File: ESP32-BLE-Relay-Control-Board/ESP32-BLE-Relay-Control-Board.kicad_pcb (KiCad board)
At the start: 2 copper layers, 13 parts, among them K1 SANYOU_SRD_Form_C, Q1 BC817, SW1 SW_Push, SW2 SW_Push, U1 ESP32-WROOM-32, U2 EL817

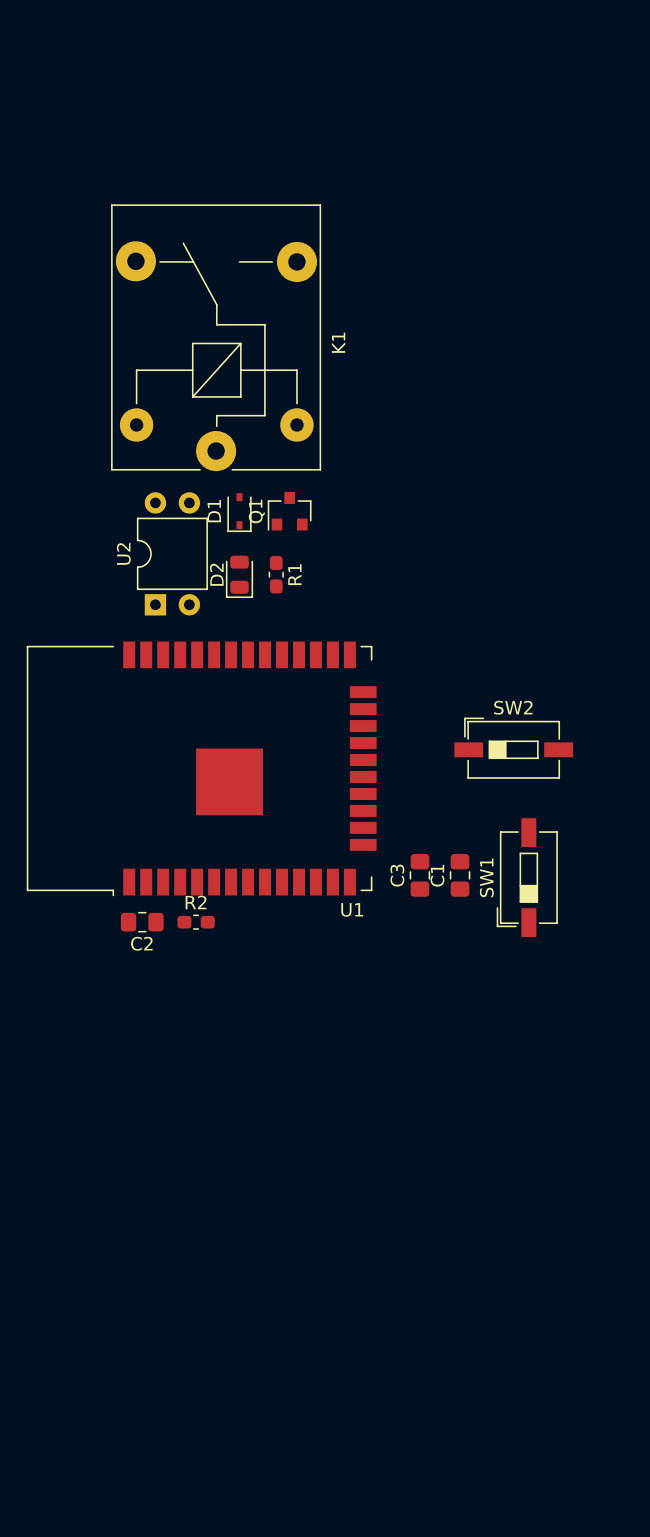
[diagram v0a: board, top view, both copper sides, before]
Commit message: relay added
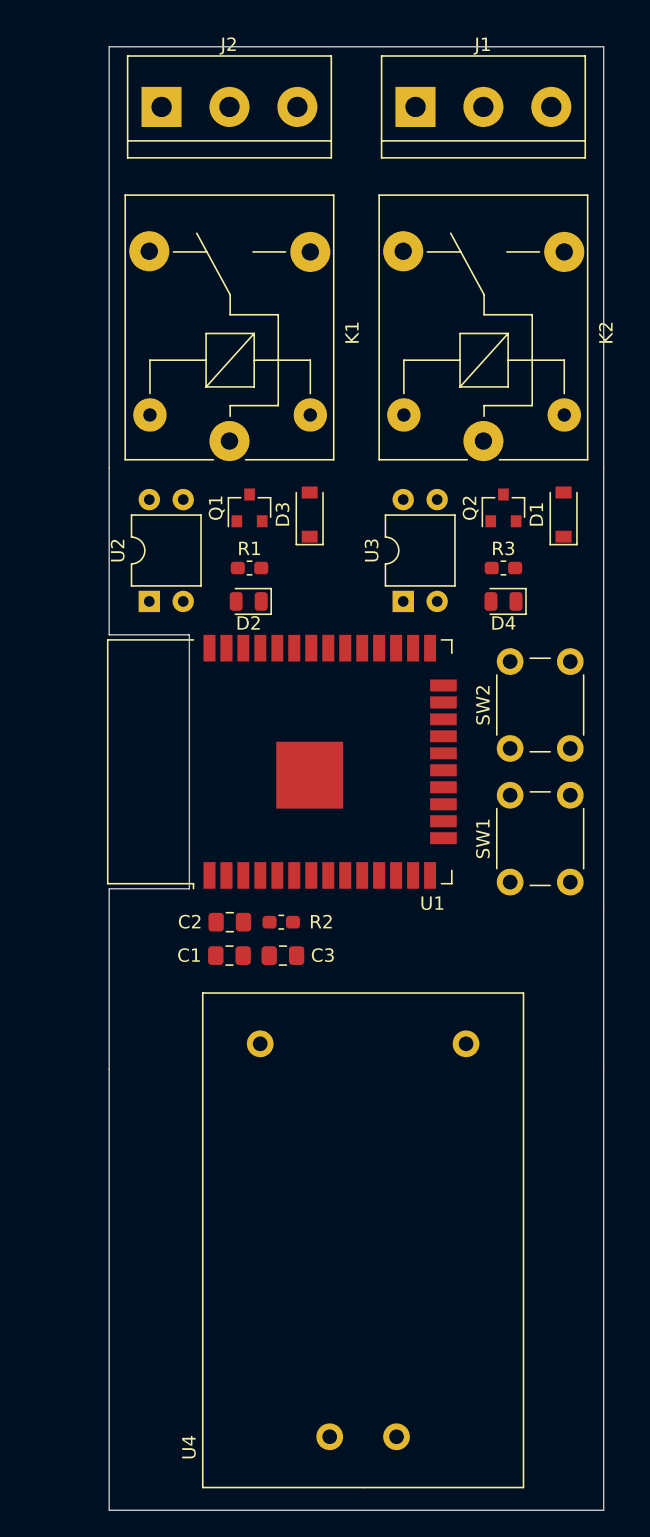
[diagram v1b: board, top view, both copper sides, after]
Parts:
- added D3: 1N4148W, Diode_SMD:D_SOD-123, F.Cu at (115.0, 103.5)
- added D4: LED, LED_SMD:LED_0805_2012Metric, F.Cu at (129.5, 110.0)
- added J1: Conn_01x03, TerminalBlock:TerminalBlock_bornier-3_P5.08mm, F.Cu at (122.9, 73.0)
- added J2: Conn_01x03, TerminalBlock:TerminalBlock_bornier-3_P5.08mm, F.Cu at (103.9, 73.0)
- added K2: SANYOU_SRD_Form_C, Relay_THT:Relay_SPDT_SANYOU_SRD_Series_Form_C, F.Cu at (128.0, 98.0)
- added Q2: BC817, Package_TO_SOT_SMD:SOT-23, F.Cu at (129.5, 103.0)
- added R3: R_Small, Resistor_SMD:R_0603_1608Metric_Pad1.05x0.95mm_HandSolder, F.Cu at (129.5, 107.5)
- added U3: EL817, Package_DIP:DIP-4_W7.62mm, F.Cu at (122.0, 110.0)
- added U4: easyPower-5V, electroShri:easyPower-5V, F.Cu at (119.0, 176.3)
- D1: value 1N4148WS -> 1N4148W; footprint Diode_SMD:D_SOD-323 -> Diode_SMD:D_SOD-123
- SW1, SW2: footprint Button_Switch_SMD:SW_DIP_SPSTx01_Slide_6.7x4.1mm_W6.73mm_P2.54mm_LowProfile_JPin -> Button_Switch_THT:SW_PUSH_6mm
- moved D1 24.3 mm to (134.0, 103.5)
- moved C1 18.3 mm to (109.0, 136.5), turned to 180 degrees
- moved C3 11.9 mm to (113.0, 136.5), turned to 0 degrees
- moved C2 6.55 mm to (109.0, 134.0)
- moved R2 6.38 mm to (112.9, 134.0)
- moved U1 6.02 mm to (115.8, 122.0)
- moved Q1 3.01 mm to (110.5, 103.0)
- moved D2 2.11 mm to (110.4, 110.0), turned to 180 degrees
- moved R1 2.06 mm to (110.5, 107.5), turned to 0 degrees
- moved SW1 1.44 mm to (130.0, 131.0)
- moved K1 1.25 mm to (109.0, 98.0)
- moved U2 0.52 mm to (103.0, 110.0)
- moved SW2 0.28 mm to (130.0, 121.0), turned to 90 degrees
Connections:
- K1 pad 1: Net-(K1-Pad1) -> /COM_2
- K1 pad 2: Net-(D1-Pad2) -> Net-(D3-Pad2)
- Q1 pad 3: Net-(D1-Pad2) -> Net-(D3-Pad2)
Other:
- board outline added: 37 x 109.5 mm

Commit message: Power in connector added
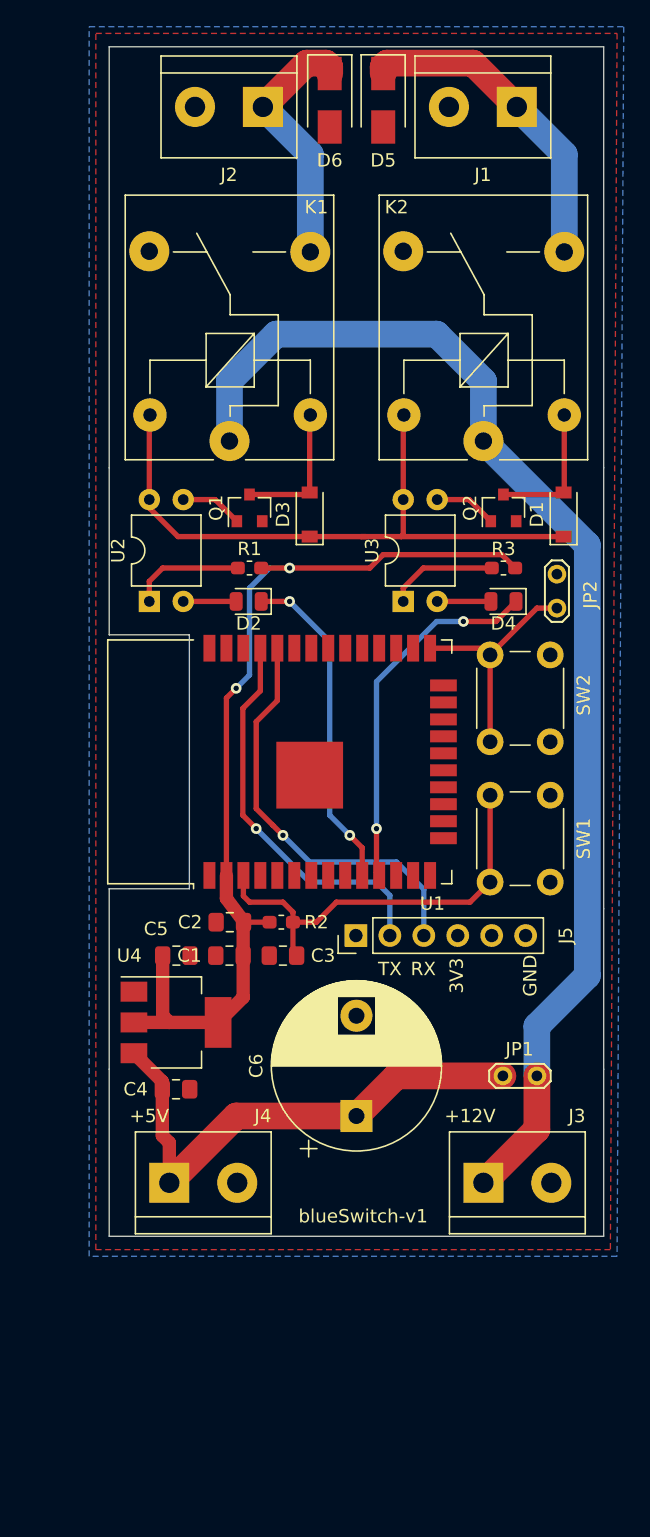
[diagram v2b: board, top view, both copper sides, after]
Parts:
- added C4: C_Small, Capacitor_SMD:C_0805_2012Metric_Pad1.15x1.40mm_HandSolder, F.Cu at (105.0, 146.5)
- added C5: C_Small, Capacitor_SMD:C_0805_2012Metric_Pad1.15x1.40mm_HandSolder, F.Cu at (105.0, 136.5)
- added C6: CP1, Capacitor_THT:CP_Radial_D12.5mm_P7.50mm, F.Cu at (118.5, 148.5)
- added D5: US1M, Diode_SMD:D_SMA, F.Cu at (120.5, 72.5)
- added D6: US1M, Diode_SMD:D_SMA, F.Cu at (116.5, 72.5)
- added J3: Screw_Terminal_01x02, TerminalBlock:TerminalBlock_bornier-2_P5.08mm, F.Cu at (128.0, 153.5)
- added J4: Screw_Terminal_01x02, TerminalBlock:TerminalBlock_bornier-2_P5.08mm, F.Cu at (104.5, 153.5)
- added J5: Conn_01x06_Female, Connector_PinHeader_2.54mm:PinHeader_1x06_P2.54mm_Vertical, F.Cu at (118.5, 135.0)
- added JP1: Jumper, TestPoint:TestPoint_2Pads_Pitch2.54mm_Drill0.8mm, F.Cu at (132.0, 145.5)
- added JP2: Jumper, TestPoint:TestPoint_2Pads_Pitch2.54mm_Drill0.8mm, F.Cu at (133.5, 110.5)
- J1, J2: value Conn_01x03 -> Screw_Terminal_01x02; footprint TerminalBlock:TerminalBlock_bornier-3_P5.08mm -> TerminalBlock:TerminalBlock_bornier-2_P5.08mm
- U4: value easyPower-5V -> LM1117-3.3; footprint electroShri:easyPower-5V -> Package_TO_SOT_SMD:SOT-223-3_TabPin2
- moved U4 37.5 mm to (105.0, 141.5), turned to 0 degrees
- moved J1 7.58 mm to (130.5, 73.0), turned to 180 degrees
- moved J2 7.58 mm to (111.5, 73.0), turned to 180 degrees
- moved SW2 1.58 mm to (128.5, 120.5)
- moved SW1 1.50 mm to (128.5, 131.0)
- turned C3 to 180 degrees
- turned R2 to 180 degrees
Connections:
- D2 pad 1: /IN1 -> IO25
- D4 pad 1: /IN2 -> IO26
- J1 pad 1: Net-(J1-Pad1) -> Net-(D5-Pad1)
- J1 pad 2: /COM_1 -> GND
- J2 pad 1: Net-(J2-Pad1) -> Net-(D6-Pad1)
- J2 pad 2: /COM_2 -> GND
- K1 pad 1: /COM_2 -> +12V
- K1 pad 3: Net-(J2-Pad3) -> Net-(D6-Pad1)
- K1 pad 4: Net-(J2-Pad1) -> Net-(K1-Pad4)
- K2 pad 1: /COM_1 -> +12V
- K2 pad 3: Net-(J1-Pad3) -> Net-(D5-Pad1)
- K2 pad 4: Net-(J1-Pad1) -> Net-(K2-Pad4)
- R1 pad 2: +5V -> +3V3
- R3 pad 2: +5V -> +3V3
- U1 pad 10: Net-(U1-Pad10) -> IO25
- U1 pad 11: Net-(U1-Pad11) -> IO26
- U1 pad 34: /RX0 -> RX0
- U1 pad 35: /TX0 -> TX0
- U4 pad 1: Net-(U4-Pad1) -> GND
- U4 pad 2: Net-(U4-Pad2) -> +3V3
- U4 pad 3: Net-(U4-Pad3) -> +5V
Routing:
- net +12V: track 0.00 -> 92.8 mm
- net +3V3: track 0.00 -> 82.6 mm, vias 0 -> 2
- net VCCQ: track 0.00 -> 48.4 mm
- net +5V: track 0.00 -> 39.1 mm
- net /EN: track 0.00 -> 31.6 mm
- net RX0: track 0.00 -> 31.2 mm, vias 0 -> 1
- net TX0: track 0.00 -> 29.5 mm, vias 0 -> 1
- net IO26: track 0.00 -> 27.5 mm, vias 0 -> 2
- net IO25: track 0.00 -> 24.9 mm, vias 0 -> 2
- net Net-(D5-Pad1): track 0.00 -> 24.3 mm
- net Net-(D6-Pad1): track 0.00 -> 19.3 mm
- net /IO0: track 0.00 -> 17.6 mm
- net Net-(D1-Pad2): track 0.00 -> 10.4 mm
- net Net-(D3-Pad2): track 0.00 -> 10.4 mm
- net Net-(R1-Pad1): track 0.00 -> 8.54 mm
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- added copper zone on B.Cu, net GND
- added copper zone on F.Cu, net GND
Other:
- board size 37 x 109.5 mm -> 37 x 89 mm
- board text added: "+12V"
- board text added: "+5V"
- board text added: "3V3"
- board text added: "GND"
- board text added: "RX"
- board text added: "TX"
- board text added: "blueSwitch-v1"

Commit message: 5V LDO Added
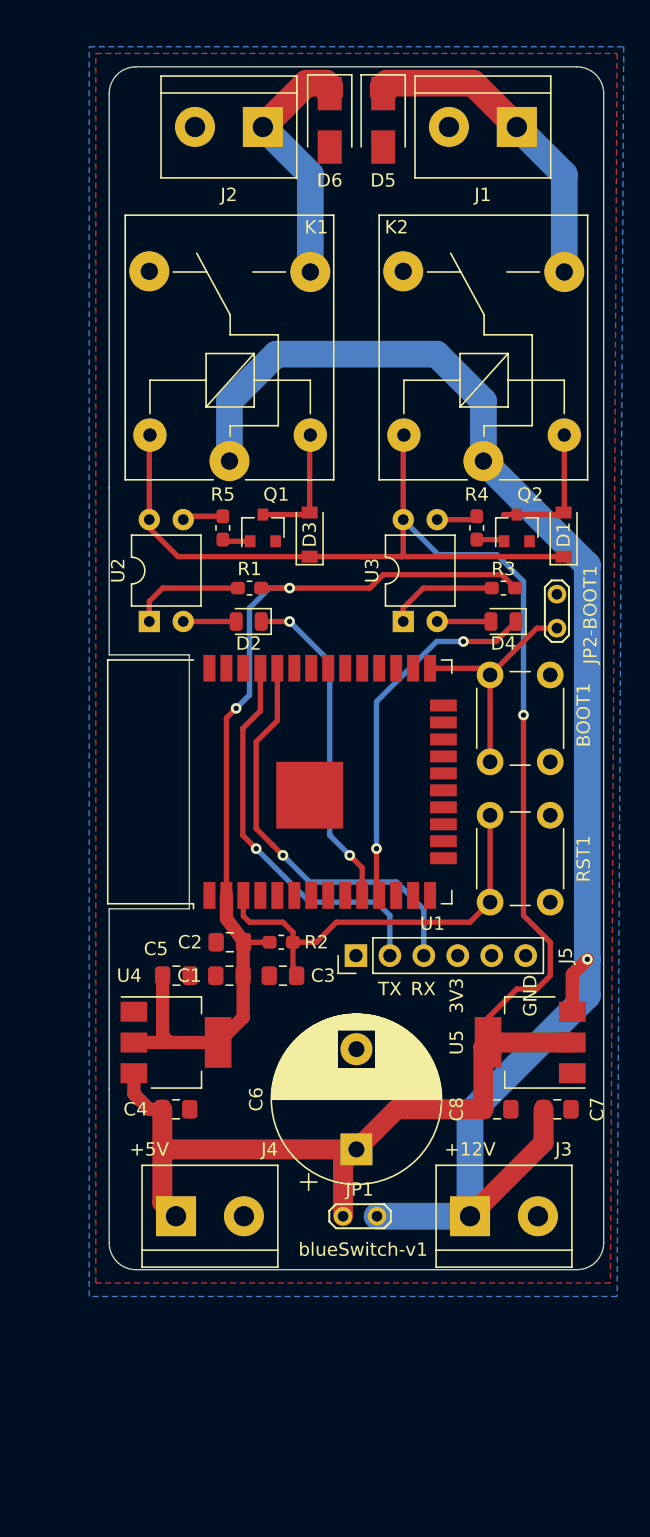
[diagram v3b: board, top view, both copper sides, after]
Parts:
- added C7: 1uF, Capacitor_SMD:C_0805_2012Metric_Pad1.15x1.40mm_HandSolder, F.Cu at (133.5, 148.0)
- added C8: 1uF, Capacitor_SMD:C_0805_2012Metric_Pad1.15x1.40mm_HandSolder, F.Cu at (129.0, 148.0)
- added R4: 500, Resistor_SMD:R_0603_1608Metric_Pad1.05x0.95mm_HandSolder, F.Cu at (127.5, 104.5)
- added R5: 500, Resistor_SMD:R_0603_1608Metric_Pad1.05x0.95mm_HandSolder, F.Cu at (108.5, 104.5)
- added U5: LM1117-5.0, Package_TO_SOT_SMD:SOT-223-3_TabPin2, F.Cu at (131.5, 143.0)
- C1, C2: value C_Small -> 0.1uF
- C4, C5: value C_Small -> 1uF
- moved JP1 15.9 mm to (120.0, 156.0)
- moved J3 2.69 mm to (127.0, 156.0)
- moved J4 2.55 mm to (105.0, 156.0)
- moved C6 2.50 mm to (118.5, 151.0)
- moved Q1 1.80 mm to (111.5, 104.5)
- moved Q2 1.80 mm to (130.5, 104.5)
- moved BOOT1 1.50 mm to (128.5, 122.0)
- moved C1 1.50 mm to (109.0, 138.0)
- moved C2 1.50 mm to (109.0, 135.5)
- moved C3 1.50 mm to (113.0, 138.0)
- moved C4 1.50 mm to (105.0, 148.0)
- moved C5 1.50 mm to (105.0, 138.0)
- moved D1 1.50 mm to (134.0, 105.0)
- moved D2 1.50 mm to (110.4, 111.5)
- moved D3 1.50 mm to (115.0, 105.0)
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- renumbered SW2 to BOOT1, JP2 to JP2-BOOT1, SW1 to RST1
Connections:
- D1 pad 1: VCCQ -> +5V
- D3 pad 1: VCCQ -> +5V
- K1 pad 5: VCCQ -> +5V
- K2 pad 5: VCCQ -> +5V
- U2 pad 3: Net-(Q1-Pad1) -> Net-(R5-Pad2)
- U2 pad 4: VCCQ -> +5V
- U3 pad 3: Net-(Q2-Pad1) -> Net-(R4-Pad2)
- U3 pad 4: VCCQ -> +5V
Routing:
- net +5V: track 39.1 -> 152.2 mm, vias 0 -> 1
- net VCCQ: track 48.4 -> 0.00 mm
- net +12V: track 92.8 -> 115.9 mm, vias 0 -> 1
- net Net-(R5-Pad2): track 0.00 -> 3.07 mm
- net Net-(R4-Pad2): track 0.00 -> 3.07 mm
- net Net-(Q1-Pad1): track 4.68 -> 2.10 mm
- net Net-(Q2-Pad1): track 4.68 -> 2.10 mm
- net Net-(D3-Pad2): track 10.4 -> 9.38 mm
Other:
- board size 37 x 89 mm -> 37 x 90 mm
